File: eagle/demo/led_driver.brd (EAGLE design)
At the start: 50 x 50 mm, 14 parts, among them T101 BC548C, X1 CLAMP_1X2-T-2.5MM, X301 MALE_2X1-T-VERTICAL, X302 CLAMP_1X2-T-2.5MM

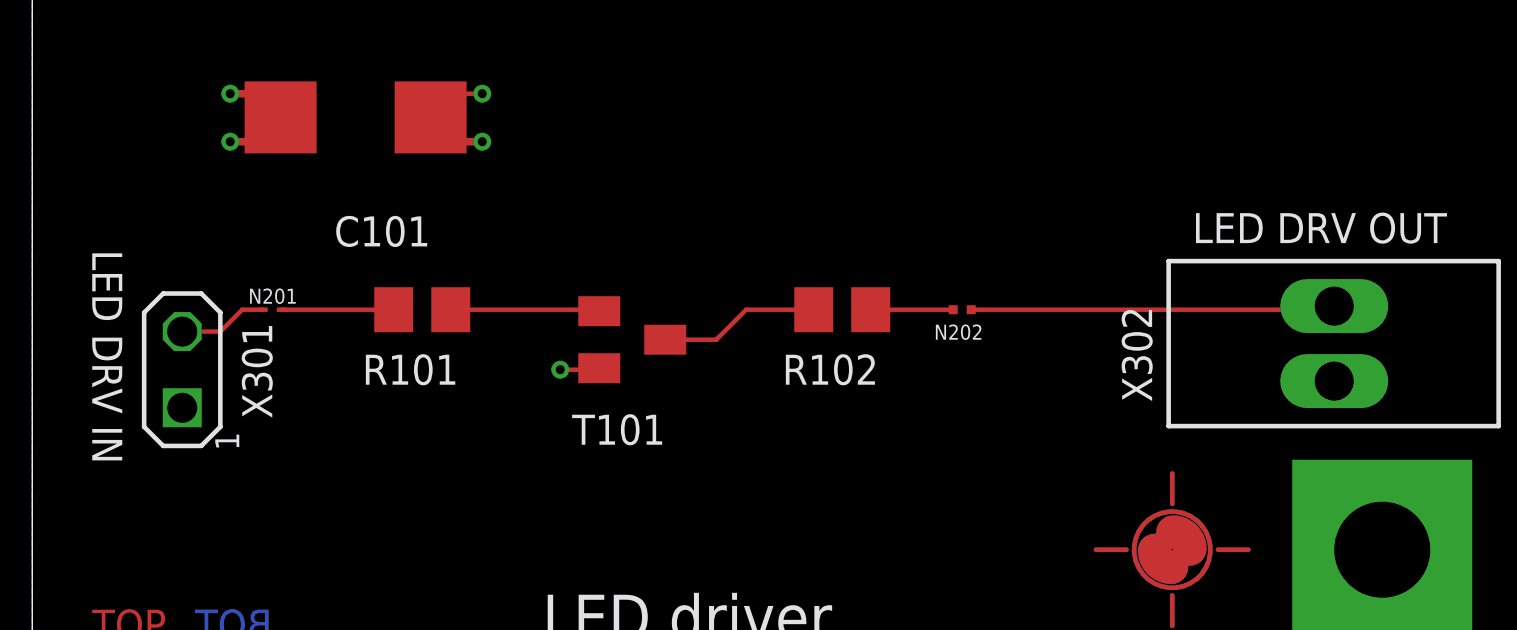
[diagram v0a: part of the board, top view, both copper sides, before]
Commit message: fixed led driver
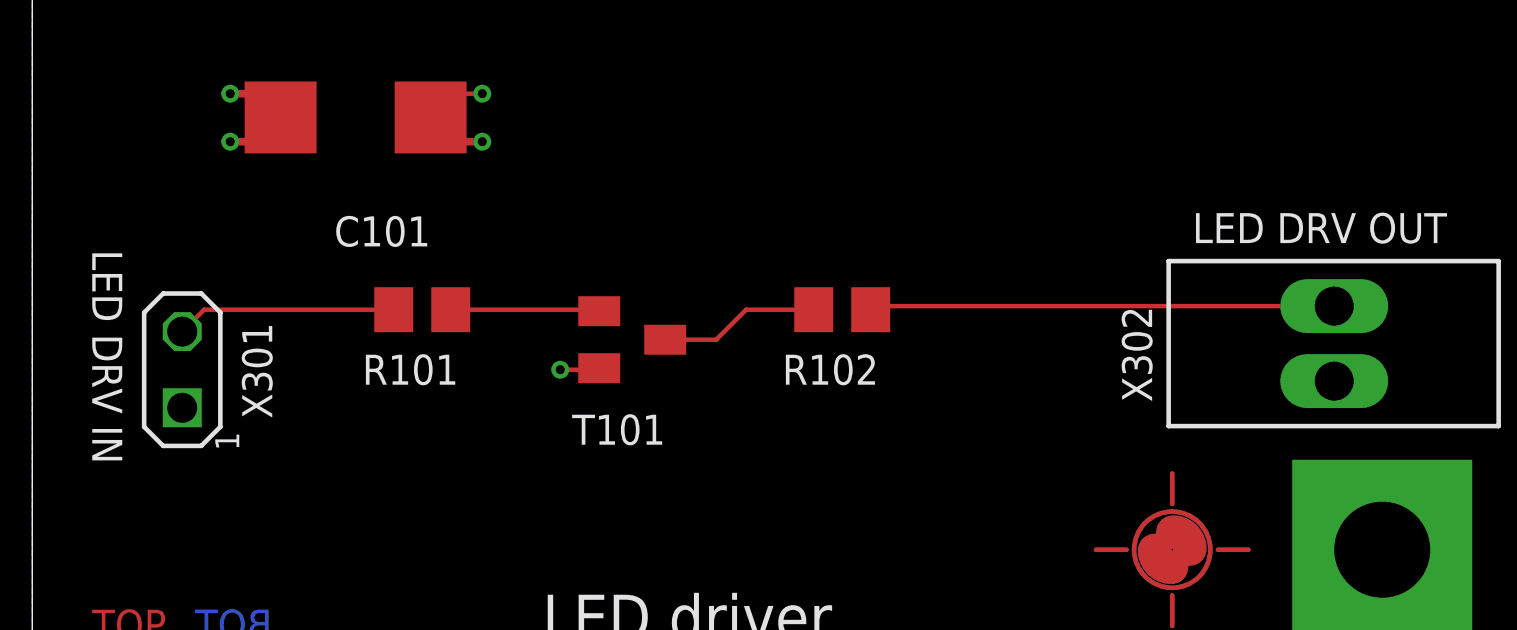
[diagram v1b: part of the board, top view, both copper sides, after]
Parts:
- removed N201: NET_CHANGER-S-0.15MM, be_con_jump:S_NET_CHANGER_0.15MM
- removed N202: NET_CHANGER-S-0.3MM, be_con_jump:S_NET_CHANGER_0.3MM
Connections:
- removed net BACKEND_DRV_IN: N201.2, X301.2
- removed net FRONTEND_DRV_OUT: N202.1, X302.2
- net DRV_IN: now also X301.2; no longer N201.1
- net DRV_OUT: now also X302.2; no longer N202.2
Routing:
- net DRV_OUT: track 2.75 -> 15.7 mm
- net FRONTEND_DRV_OUT: track 12.1 -> 0.00 mm
- net DRV_IN: track 3.75 -> 7.35 mm
- net BACKEND_DRV_IN: track 3.00 -> 0.00 mm
- added copper zone on layer 2, net P5V
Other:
- board text added: "L2"
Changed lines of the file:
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@@
 <setting verticaltext="up"/>
 </settings>
-<grid distance="5" unitdist="mm" unit="mm" style="lines" multiple="1" display="yes" altdistance="0.2" altunitdist="mm" altunit="mm"/>
+<grid distance="1" unitdist="mm" unit="mm" style="lines" multiple="1" display="yes" altdistance="0.2" altunitdist="mm" altunit="mm"/>
 <layers>
 <layer number="1" name="Top" color="4" fill="1" visible="yes" active="yes"/>
-<layer number="2" name="Route2" color="1" fill="3" visible="no" active="yes"/>
+<layer number="2" name="Route2" color="1" fill="3" visible="yes" active="yes"/>
 <layer number="3" name="Route3" color="4" fill="3" visible="no" active="no"/>
 <layer number="4" name="Route4" color="1" fill="4" visible="no" active="no"/>
@@
 <layer number="13" name="Route13" color="4" fill="5" visible="no" active="no"/>
 <layer number="14" name="Route14" color="1" fill="6" visible="no" active="no"/>
-<layer number="15" name="Route15" color="4" fill="6" visible="no" active="yes"/>
-<layer number="16" name="Bottom" color="1" fill="1" visible="yes" active="yes"/>
+<layer number="15" name="Route15" color="4" fill="6" visible="yes" active="yes"/>
+<layer number="16" name="Bottom" color="1" fill="1" visible="no" active="yes"/>
 <layer number="17" name="Pads" color="2" fill="1" visible="yes" active="yes"/>
 <layer number="18" name="Vias" color="2" fill="1" visible="yes" active="yes"/>
@@
 <dimension x1="50" y1="50" x2="50" y2="0" x3="65" y3="25" textsize="1.5" textratio="13" layer="47"/>
 <dimension x1="45" y1="45" x2="45" y2="5" x3="60" y3="25" textsize="1.5" textratio="13" layer="47"/>
+<text x="38" y="46" size="1" layer="2" font="vector" ratio="13">L2</text>
 </plain>
 <attributes>
@@
 <attribute name="VALUE" x="13.28" y="17.41" size="1" layer="27" font="vector" ratio="13" rot="R180"/>
 </element>
-<element name="N201" library="be_con_jump" package="S_NET_CHANGER_0.15MM" value="NET_CHANGER-S-0.15MM" x="8" y="13" smashed="yes" rot="R180">
-<attribute name="FUNCTION" value="" x="8" y="13" size="1.778" layer="27" rot="R180" display="off"/>
-<attribute name="PART_CODE_EXT" value="" x="8" y="13" size="1.778" layer="27" rot="R180" display="off"/>
-<attribute name="COMMISSIONED" value="2013-08-30" x="8" y="13" size="1.778" layer="27" rot="R180" display="off"/>
-<attribute name="BOM" value="NO" x="8" y="13" size="1.778" layer="27" rot="R180" display="off"/>
-<attribute name="PART_CODE_BEL" value="N_PAC_S_NET_CHANGER_0.15MM" x="8" y="13" size="1.778" layer="27" rot="R180" display="off"/>
-<attribute name="UPDATED" value="" x="8" y="13" size="1.778" layer="27" rot="R180" display="off"/>
-<attribute name="NAME" x="7.2" y="13.2" size="0.5" layer="25" font="vector" ratio="13"/>
-</element>
-<element name="N202" library="be_con_jump" package="S_NET_CHANGER_0.3MM" value="NET_CHANGER-S-0.3MM" x="31" y="13" smashed="yes" rot="R180">
-<attribute name="FUNCTION" value="" x="31" y="13" size="1.778" layer="27" rot="R180" display="off"/>
-<attribute name="PART_CODE_EXT" value="" x="31" y="13" size="1.778" layer="27" rot="R180" display="off"/>
-<attribute name="COMMISSIONED" value="2014-04-09" x="31" y="13" size="1.778" layer="27" rot="R180" display="off"/>
-<attribute name="BOM" value="NO" x="31" y="13" size="1.778" layer="27" rot="R180" display="off"/>
-<attribute name="PART_CODE_BEL" value="N_PAC_S_NET_CHANGER_0.3MM" x="31" y="13" size="1.778" layer="27" rot="R180" display="off"/>
-<attribute name="UPDATED" value="" x="31" y="13" size="1.778" layer="27" rot="R180" display="off"/>
-<attribute name="NAME" x="31.7" y="12.5" size="0.5" layer="25" font="vector" ratio="13" rot="R180"/>
-</element>
 <element name="R101" library="be_rcl" package="S_0805" value="2k2" x="13" y="13" smashed="yes">
 <attribute name="FUNCTION" value="" x="13" y="13" size="1.778" layer="27" display="off"/>
@@
 <contactref element="X302" pad="1"/>
 <contactref element="X1" pad="2"/>
-<wire x1="19.75" y1="42.02" x2="43.4" y2="10.62" width="0" layer="19" extent="1-1"/>
-<wire x1="15" y1="20.2" x2="19.75" y2="42.02" width="0" layer="19" extent="1-1"/>
+<polygon width="0.15" layer="2">
+<vertex x="11" y="50"/>
+<vertex x="50" y="50"/>
+<vertex x="50" y="7"/>
+<vertex x="11" y="7"/>
+</polygon>
 </signal>
 <signal name="GND">
@@
 <signal name="DRV_IN">
 <contactref element="R101" pad="1"/>
-<contactref element="N201" pad="1"/>
-<wire x1="8.3" y1="13" x2="12.05" y2="13" width="0.15" layer="1"/>
+<contactref element="X301" pad="2"/>
+<wire x1="5" y1="12.27" x2="5.73" y2="13" width="0.15" layer="1"/>
+<wire x1="5.73" y1="13" x2="12.05" y2="13" width="0.15" layer="1"/>
 </signal>
 <signal name="DRV_B">
@@
 <signal name="DRV_OUT">
 <contactref element="R102" pad="2"/>
-<contactref element="N202" pad="2"/>
-<wire x1="27.95" y1="13" x2="30.7" y2="13" width="0.15" layer="1"/>
-</signal>
-<signal name="BACKEND_DRV_IN">
-<contactref element="N201" pad="2"/>
-<contactref element="X301" pad="2"/>
-<wire x1="5" y1="12.27" x2="6.27" y2="12.27" width="0.15" layer="1"/>
-<wire x1="6.27" y1="12.27" x2="7" y2="13" width="0.15" layer="1"/>
-<wire x1="7" y1="13" x2="7.7" y2="13" width="0.15" layer="1"/>
-</signal>
-<signal name="FRONTEND_DRV_OUT">
-<contactref element="N202" pad="1"/>
 <contactref element="X302" pad="2"/>
-<wire x1="31.3" y1="13" x2="43.28" y2="13" width="0.15" layer="1"/>
 <wire x1="43.28" y1="13" x2="43.4" y2="13.12" width="0.15" layer="1"/>
+<wire x1="27.95" y1="13" x2="27.95" y2="13.12" width="0.15" layer="1"/>
+<wire x1="27.95" y1="13.12" x2="43.4" y2="13.12" width="0.15" layer="1"/>
 </signal>
 </signals>

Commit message: fixed prefixes
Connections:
- net DRV_B renamed LED_DRV_B
- net DRV_C renamed LED_DRV_C
- net DRV_IN renamed LED_DRV_IN
- net DRV_OUT renamed LED_DRV_OUT
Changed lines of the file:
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@@
 <contactref element="X1" pad="1"/>
 </signal>
-<signal name="DRV_IN">
+<signal name="LED_DRV_IN">
 <contactref element="R101" pad="1"/>
 <contactref element="X301" pad="2"/>
@@
 <wire x1="5.73" y1="13" x2="12.05" y2="13" width="0.15" layer="1"/>
 </signal>
-<signal name="DRV_B">
+<signal name="LED_DRV_B">
 <contactref element="R101" pad="2"/>
 <contactref element="T101" pad="1"/>
@@
 <wire x1="18.85" y1="13" x2="18.9" y2="12.95" width="0.15" layer="1"/>
 </signal>
-<signal name="DRV_C">
+<signal name="LED_DRV_C">
 <contactref element="T101" pad="3"/>
 <contactref element="R102" pad="1"/>
@@
 <wire x1="23.8" y1="13" x2="26.05" y2="13" width="0.15" layer="1"/>
 </signal>
-<signal name="DRV_OUT">
+<signal name="LED_DRV_OUT">
 <contactref element="R102" pad="2"/>
 <contactref element="X302" pad="2"/>

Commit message: fix partcodes
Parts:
- removed X1: CLAMP_1X2-T-2.5MM, be_con_jump:T_WIRE_CLAMP_1X2_PITCH_2MM5
- added X201: MALE_2X1-T-VERTICAL, be_con_jump:T_MALE_2X1_VERTICAL_PITCH_2MM54
- C101: value 100n -> 10u
- T101: value BC548C -> BCW60D
- X301: value MALE_2X1-T-VERTICAL -> CLAMP_1X2-T-2.5MM; device be_con_jump:T_MALE_2X1_VERTICAL_PITCH_2MM54 -> be_con_jump:T_WIRE_CLAMP_1X2_PITCH_2MM5
- moved X301 34.9 mm to (21.0, 42.0), turned to 180 degrees
- renumbered X302 to X101
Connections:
- net GND: now also X201.1; no longer X1.1
- net LED_DRV_IN: now also X201.2; no longer X301.2
- net P5V: now also X301.2; no longer X1.2
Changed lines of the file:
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@@
 </autorouter>
 <elements>
-<element name="C101" library="be_rcl" package="S_6032" value="100n" x="10.78" y="19.41" smashed="yes" rot="R180">
+<element name="C101" library="be_rcl" package="S_6032" value="10u" x="10.78" y="19.41" smashed="yes" rot="R180">
 <attribute name="FUNCTION" value="" x="10.78" y="19.41" size="1.778" layer="27" rot="R180" display="off"/>
 <attribute name="PART_CODE_EXT" value="" x="10.78" y="19.41" size="1.778" layer="27" rot="R180" display="off"/>
 <attribute name="COMMISSIONED" value="2013-08-30" x="10.78" y="19.41" size="1.778" layer="27" rot="R180" display="off"/>
 <attribute name="BOM" value="YES" x="10.78" y="19.41" size="1.778" layer="27" rot="R180" display="off"/>
-<attribute name="PART_CODE_BEL" value="C_PAC_S_6032_VAL_" x="10.78" y="19.41" size="1.778" layer="27" rot="R180" display="off"/>
+<attribute name="PART_CODE_BEL" value="C_PAC_S_6032_VAL_10u_Vmax_35V" x="10.78" y="19.41" size="1.778" layer="27" rot="R180" display="off"/>
 <attribute name="UPDATED" value="" x="10.78" y="19.41" size="1.778" layer="27" rot="R180" display="off"/>
 <attribute name="NAME" x="13.28" y="16.11" size="1" layer="25" font="vector" ratio="13" rot="R180"/>
@@
 <attribute name="COMMISSIONED" value="2013-08-30" x="13" y="13" size="1.778" layer="27" display="off"/>
 <attribute name="BOM" value="YES" x="13" y="13" size="1.778" layer="27" display="off"/>
-<attribute name="PART_CODE_BEL" value="R_PAC_S_0805_VAL_" x="13" y="13" size="1.778" layer="27" display="off"/>
+<attribute name="PART_CODE_BEL" value="R_PAC_S_0805_VAL_2k2" x="13" y="13" size="1.778" layer="27" display="off"/>
 <attribute name="UPDATED" value="" x="13" y="13" size="1.778" layer="27" display="off"/>
 <attribute name="NAME" x="11" y="10.5" size="1" layer="25" font="vector" ratio="13"/>
@@
 <attribute name="COMMISSIONED" value="2013-08-30" x="27" y="13" size="1.778" layer="27" display="off"/>
 <attribute name="BOM" value="YES" x="27" y="13" size="1.778" layer="27" display="off"/>
-<attribute name="PART_CODE_BEL" value="R_PAC_S_0805_VAL_" x="27" y="13" size="1.778" layer="27" display="off"/>
+<attribute name="PART_CODE_BEL" value="R_PAC_S_0805_VAL_100" x="27" y="13" size="1.778" layer="27" display="off"/>
 <attribute name="UPDATED" value="" x="27" y="13" size="1.778" layer="27" display="off"/>
 <attribute name="NAME" x="25" y="10.5" size="1" layer="25" font="vector" ratio="13"/>
 <attribute name="VALUE" x="25" y="9" size="1" layer="27" font="vector" ratio="13"/>
 </element>
-<element name="T101" library="be_transistor" package="S_SOT23" value="BC548C" x="20" y="12" smashed="yes" rot="R270">
+<element name="T101" library="be_transistor" package="S_SOT23" value="BCW60D" x="20" y="12" smashed="yes" rot="R270">
 <attribute name="FUNCTION" value="" x="20" y="12" size="1.778" layer="27" rot="R270" display="off"/>
 <attribute name="PART_CODE_EXT" value="" x="20" y="12" size="1.778" layer="27" rot="R270" display="off"/>
 <attribute name="COMMISSIONED" value="2013-08-30" x="20" y="12" size="1.778" layer="27" rot="R270" display="off"/>
 <attribute name="BOM" value="YES" x="20" y="12" size="1.778" layer="27" rot="R270" display="off"/>
-<attribute name="PART_CODE_BEL" value="T_PAC_S_SOT23_VAL_" x="20" y="12" size="1.778" layer="27" rot="R270" display="off"/>
+<attribute name="PART_CODE_BEL" value="T_PAC_S_SOT23_VAL_BCW60D" x="20" y="12" size="1.778" layer="27" rot="R270" display="off"/>
 <attribute name="UPDATED" value="" x="20" y="12" size="1.778" layer="27" rot="R270" display="off"/>
 <attribute name="NAME" x="18" y="8.5" size="1" layer="25" font="vector" ratio="13"/>
 <attribute name="VALUE" x="18" y="7" size="1" layer="27" font="vector" ratio="13"/>
 </element>
-<element name="X302" library="be_con_jump" package="T_WIRE_CLAMP_1X2_PITCH_2MM5" value="CLAMP_1X2-T-2.5MM" x="43.38" y="11.87" smashed="yes" rot="R90">
+<element name="X101" library="be_con_jump" package="T_WIRE_CLAMP_1X2_PITCH_2MM5" value="CLAMP_1X2-T-2.5MM" x="43.38" y="11.87" smashed="yes" rot="R90">
 <attribute name="FUNCTION" value="LED DRV OUT" x="38.67" y="15.22" size="1" layer="21" font="vector" ratio="15"/>
 <attribute name="PART_CODE_EXT" value="" x="43.38" y="11.87" size="1.778" layer="27" rot="R90" display="off"/>
@@
 <attribute name="NAME" x="37.33" y="9.92" size="1" layer="25" font="vector" ratio="15" rot="R90"/>
 </element>
-<element name="X301" library="be_con_jump" package="T_MALE_2X1_VERTICAL_PITCH_2MM54" value="MALE_2X1-T-VERTICAL" x="5" y="11" smashed="yes">
+<element name="X201" library="be_con_jump" package="T_MALE_2X1_VERTICAL_PITCH_2MM54" value="MALE_2X1-T-VERTICAL" x="5" y="11" smashed="yes">
 <attribute name="FUNCTION" value="LED DRV IN" x="2" y="15" size="1" layer="21" font="vector" ratio="15" rot="SR270"/>
 <attribute name="PART_CODE_EXT" value="" x="5" y="11" size="1.778" layer="27" display="off"/>
@@
 <attribute name="UPDATED" value="" x="45" y="5" size="1" layer="27" font="vector" ratio="15" display="off"/>
 </element>
-<element name="X1" library="be_con_jump" package="T_WIRE_CLAMP_1X2_PITCH_2MM5" value="CLAMP_1X2-T-2.5MM" x="21" y="42" smashed="yes" rot="R180">
+<element name="X301" library="be_con_jump" package="T_WIRE_CLAMP_1X2_PITCH_2MM5" value="CLAMP_1X2-T-2.5MM" x="21" y="42" smashed="yes" rot="R180">
 <attribute name="FUNCTION" value="PWR IN" x="24.4" y="44.8" size="1" layer="21" font="vector" ratio="15" rot="R270"/>
 <attribute name="PART_CODE_EXT" value="" x="21" y="42" size="1" layer="27" font="vector" ratio="15" rot="R180" display="off"/>
@@
 <wire x1="14" y1="20.2" x2="15" y2="20.2" width="0.15" layer="1"/>
 <via x="15" y="20.2" extent="1-16" drill="0.3"/>
-<contactref element="X302" pad="1"/>
-<contactref element="X1" pad="2"/>
+<contactref element="X101" pad="1"/>
+<contactref element="X301" pad="2"/>
 <polygon width="0.15" layer="2">
 <vertex x="11" y="50"/>
@@
 <contactref element="T101" pad="2"/>
 <contactref element="C101" pad="-"/>
-<contactref element="X301" pad="1"/>
+<contactref element="X201" pad="1"/>
 <wire x1="8.28" y1="19.41" x2="8.28" y2="18.6" width="0.254" layer="1"/>
 <wire x1="8.28" y1="18.6" x2="6.6" y2="18.6" width="0.254" layer="1"/>
@@
 <wire x1="18.9" y1="11" x2="17.6" y2="11" width="0.15" layer="1"/>
 <via x="17.6" y="11" extent="1-16" drill="0.3"/>
-<contactref element="X1" pad="1"/>
+<contactref element="X301" pad="1"/>
 </signal>
 <signal name="LED_DRV_IN">
 <contactref element="R101" pad="1"/>
-<contactref element="X301" pad="2"/>
+<contactref element="X201" pad="2"/>
 <wire x1="5" y1="12.27" x2="5.73" y2="13" width="0.15" layer="1"/>
 <wire x1="5.73" y1="13" x2="12.05" y2="13" width="0.15" layer="1"/>
@@
 <signal name="LED_DRV_OUT">
 <contactref element="R102" pad="2"/>
-<contactref element="X302" pad="2"/>
+<contactref element="X101" pad="2"/>
 <wire x1="43.28" y1="13" x2="43.4" y2="13.12" width="0.15" layer="1"/>
 <wire x1="27.95" y1="13" x2="27.95" y2="13.12" width="0.15" layer="1"/>
